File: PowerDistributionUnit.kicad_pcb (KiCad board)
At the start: 4 copper layers, 179.3 x 86.6 mm, 113 parts, among them J1.1 POWER_PINS, J1.10 RF_PINS, J1.11 EPS_PINS, J1.12 I_BAT_PINS, J1.13 I_PV_PINS, J1.2 UART_PINS, J1.3 SBW_PINS, J1.4 I2C_PINS, J1.5 30_Minute_Bypass_Jumpers, J1.6 Direct_Power_Pins, J1.7 OBC_PINS, J1.8 PL_PINS, J1.9 ACS_PINS, M1.1 PMOS, M1.2 PMOS, M1.3 NMOS, M1.4 PMOS, SW1.1 Inhibit, SW1.2 Inhibit, U1.1 LTC6995, U2.1 MSP430F5529IPN, U3.1 RT4812, U4.1 TPS62086, U5.1 TPS2557, U5.2 TPS2557, U5.3 TPS2557, U5.4 TPS2557, U6.1 MAX44284E, U6.2 MAX44284E, U6.3 MAX44284E, U6.4 MAX44284E, U6.5 MAX44284E, U6.6 MAX44284E, U6.7 MAX44284E

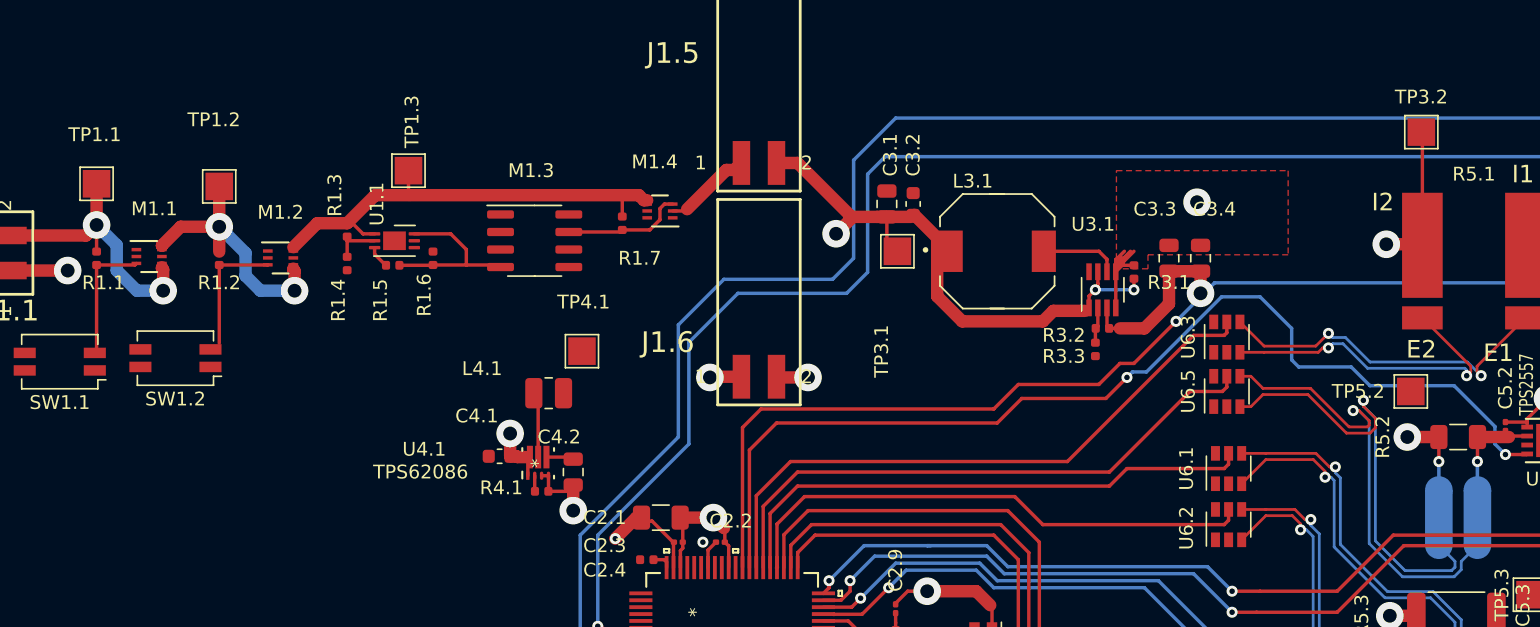
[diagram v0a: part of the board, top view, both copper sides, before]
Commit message: Adjusted power plane and added missing ground VIAs
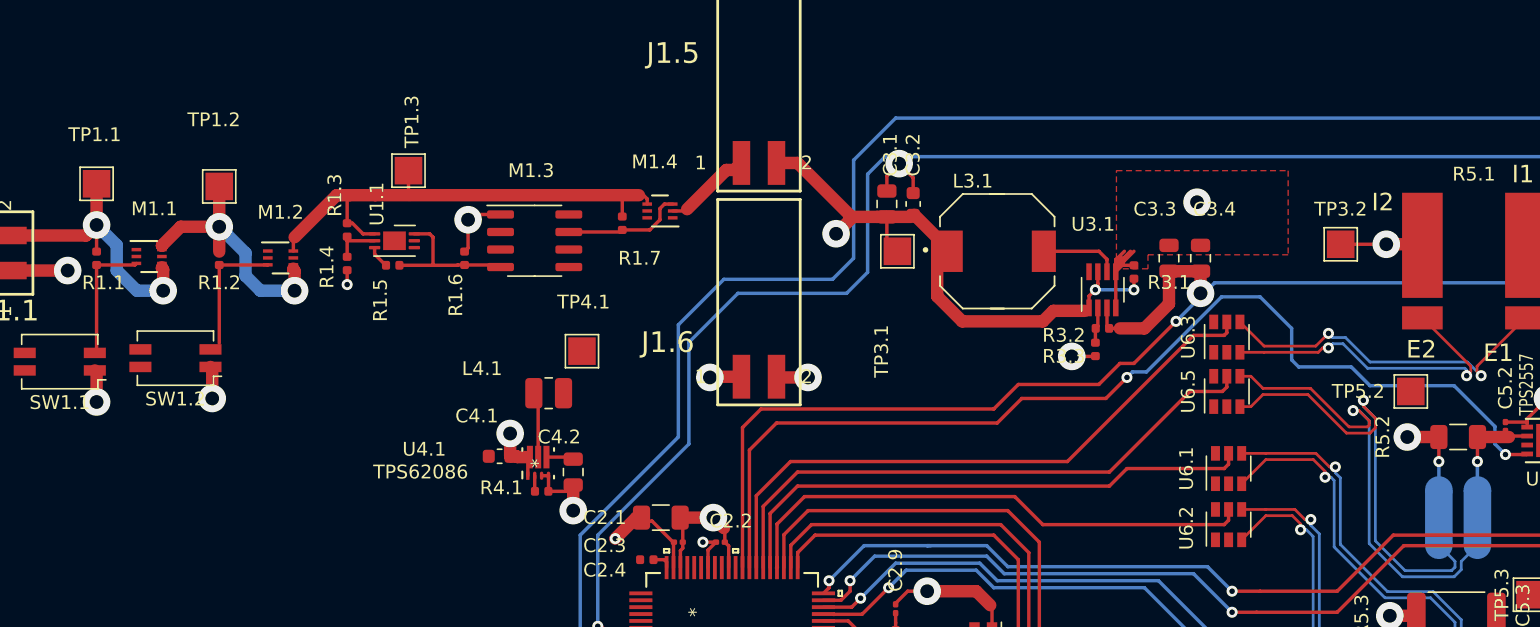
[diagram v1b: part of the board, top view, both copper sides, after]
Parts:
- moved TP3.2 10.0 mm to (174.5, 77.0)
- moved R1.6 2.29 mm to (111.0, 78.0)
- turned R1.4 to 270 degrees
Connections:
- C2.1 pad 1 (DVCC1): (no net) -> /3.3V_Regulated
- C2.2 pad 1: 3.3V_MSP -> /3.3V_Regulated
- C2.3 pad 1 (DVCC1): (no net) -> /3.3V_Regulated
- C2.5 pad 1 (VBUS): (no net) -> /5V_Regulated
- C3.1 pad 1: /30_Minute_Output -> Net-(J1.5-Pad2)
- C3.2 pad 1: /30_Minute_Output -> Net-(J1.5-Pad2)
- C4.1 pad 1: /30_Minute_Output -> Net-(J1.5-Pad2)
- J1.1 pad 1: Net-(J1.1-Pad1) -> GNDA
- J1.1 pad 2: GNDA -> Net-(J1.1-Pad1)
- J1.6 pad 1: /30_Minute_Output -> Net-(J1.5-Pad2)
- L3.1 pad 1: /30_Minute_Output -> Net-(J1.5-Pad2)
- M1.2 pad 6 (D): (no net) -> Net-(M1.2-Pad2)
- M1.3 pad 1 (S): (no net) -> GNDA
- M1.3 pad 4 (G): (no net) -> Net-(M1.3-Pad2)
- M1.4 pad 4 (S): (no net) -> Net-(M1.2-Pad2)
- R1.3 pad 1: Net-(M1.2-Pad1) -> Net-(M1.2-Pad2)
- TP3.1 pad 1: /30_Minute_Output -> Net-(J1.5-Pad2)
- U1.1 pad 6 (OUT): (no net) -> Net-(M1.3-Pad2)
- U2.1 pad 11 (AVCC1): (no net) -> /3.3V_Regulated
- U2.1 pad 14 (AVSS1): (no net) -> GNDA
- U2.1 pad 18 (DVCC1): (no net) -> /3.3V_Regulated
- U2.1 pad 65 (VBUS): (no net) -> /5V_Regulated
- U4.1 pad 1 (EN): (no net) -> Net-(J1.5-Pad2)
- U4.1 pad 7 (VIN): (no net) -> Net-(J1.5-Pad2)
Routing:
- net GNDA: track 141.6 -> 166.7 mm, vias 12 -> 19
- net 3.3V_MSP: track 11.0 -> 1.03 mm, vias 2 -> 1
- net /3.3V_Regulated: track 7.82 -> 17.8 mm, vias 2 -> 3
- net (no net): track 15.8 -> 8.31 mm, vias 1 -> 0
- net /30_Minute_Output: track 13.4 -> 6.83 mm, vias 2 -> 0
- net Net-(J1.5-Pad2): track 42.4 -> 49.0 mm, vias 3 -> 5
- net Net-(J1.1-Pad1): track 26.4 -> 21.7 mm, vias 3 -> 2
- net Net-(M1.2-Pad2): track 33.0 -> 36.1 mm
- net /5V_Regulated: track 43.0 -> 45.7 mm, vias 11 -> 12
- net GND: track 2.08 -> 0.00 mm
- net Net-(M1.3-Pad2): track 12.8 -> 10.9 mm

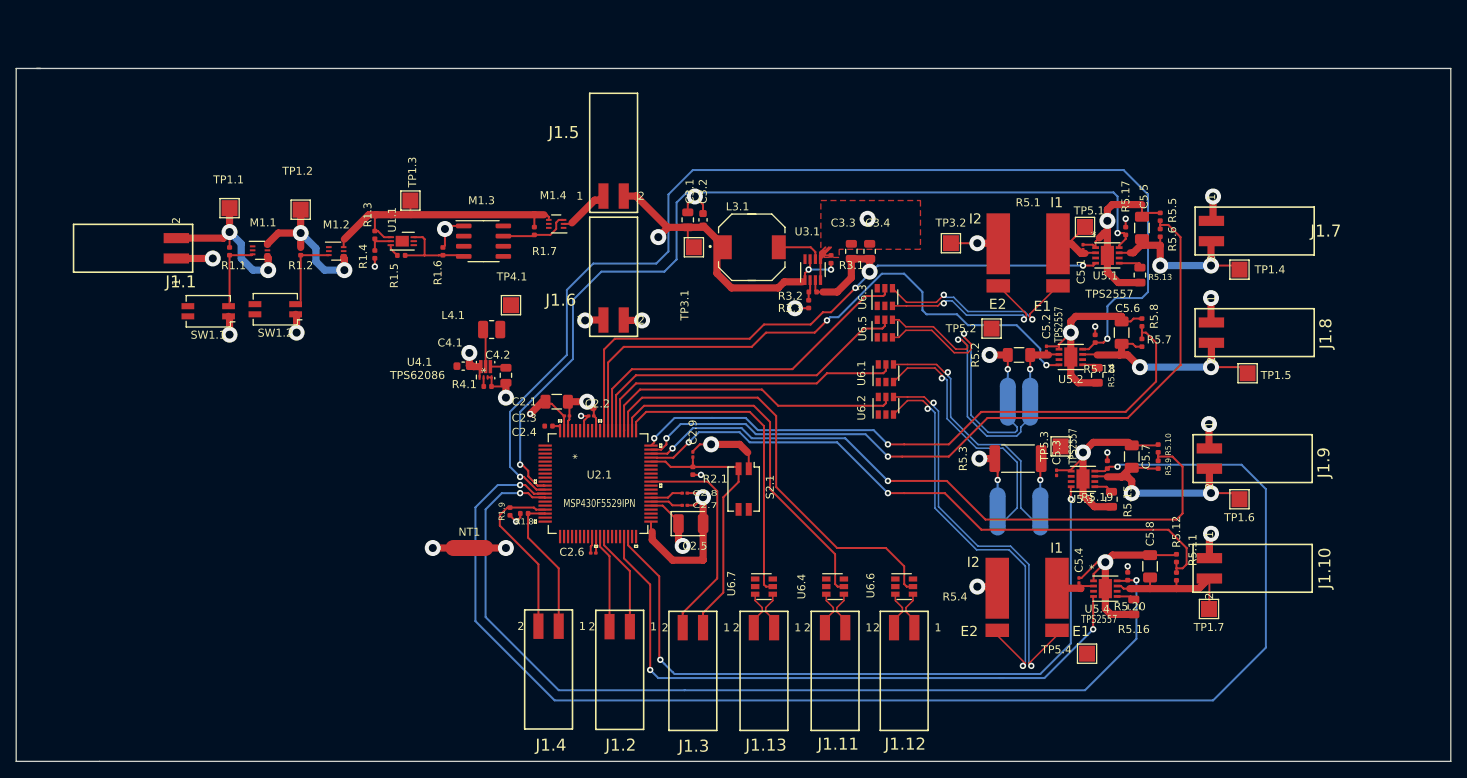
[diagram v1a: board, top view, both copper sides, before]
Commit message: Changed board outline to reflect CubeSat dimensions
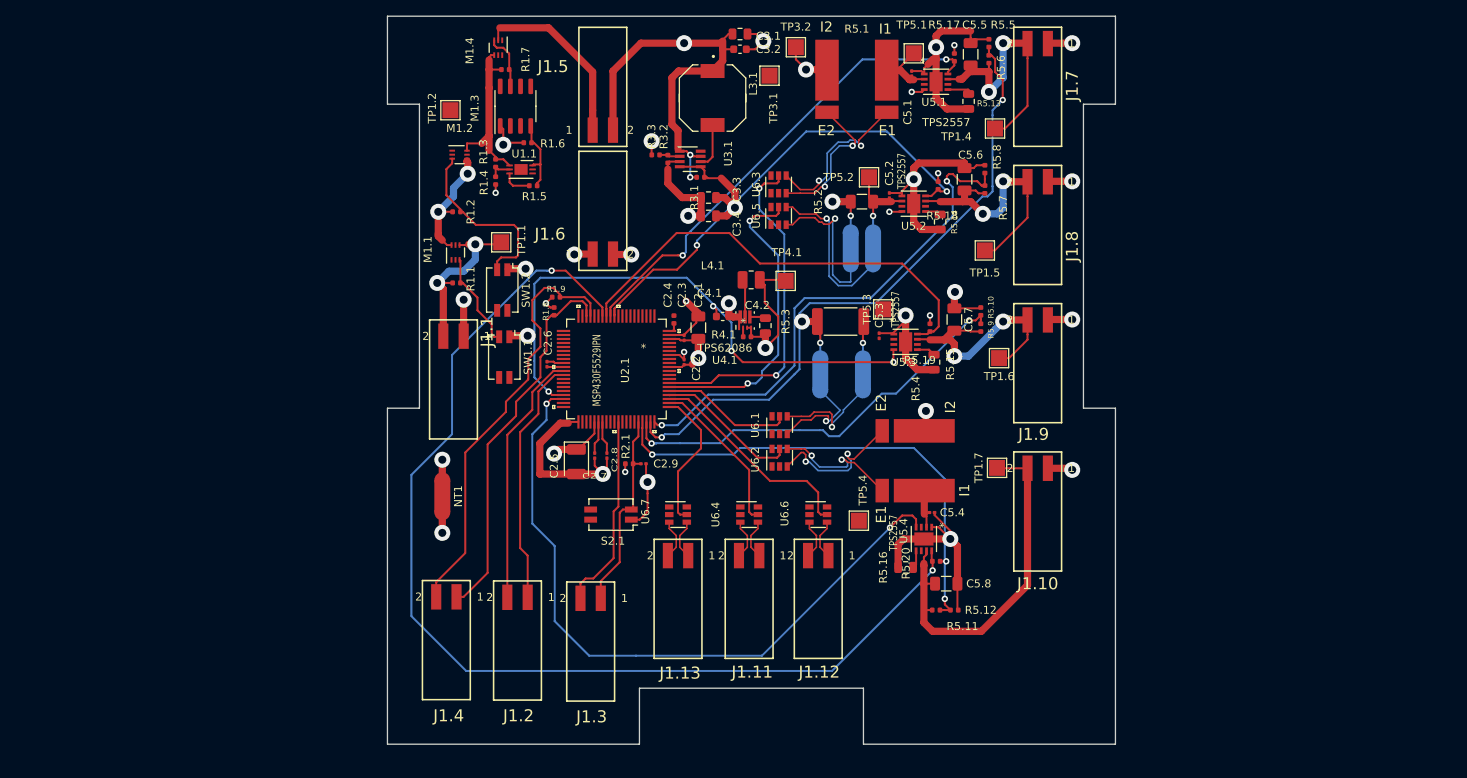
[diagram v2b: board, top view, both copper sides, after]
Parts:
- removed TP1.3: LTC_TP, TestPoint:TestPoint_Pad_2.0x2.0mm
- moved J1.1 43.1 mm to (112.3, 93.9), turned to 180 degrees
- moved SW1.1 37.4 mm to (118.7, 91.2), turned to 270 degrees
- moved TP1.5 36.3 mm to (178.7, 77.9)
- moved TP1.4 35.3 mm to (180.0, 62.6)
- moved TP1.6 34.8 mm to (180.5, 91.3)
- moved TP4.1 34.5 mm to (153.8, 81.7)
- moved TP1.1 34.2 mm to (118.3, 76.8), turned to 90 degrees
- moved L4.1 33.0 mm to (149.5, 81.5)
- moved U4.1 33.0 mm to (148.8, 86.6)
- moved C4.1 33.0 mm to (146.0, 86.1)
- moved C4.2 33.0 mm to (151.3, 87.3)
- moved R4.1 33.0 mm to (149.0, 88.7)
- moved TP5.4 33.0 mm to (163.0, 111.6), turned to 270 degrees
- moved J1.7 32.5 mm to (185.3, 57.3), turned to 180 degrees
- moved TP1.7 31.8 mm to (180.3, 105.0), turned to 270 degrees
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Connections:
- C5.8 pad 1: Net-(C5.8-Pad1) -> /SubsystemLoadSwitches/RF
- M1.1 pad 4 (S): (no net) -> Net-(J1.1-Pad1)
- M1.1 pad 6 (D): (no net) -> Net-(M1.1-Pad1)
- M1.2 pad 3 (G): (no net) -> Net-(M1.2-Pad1)
- M1.2 pad 4 (S): (no net) -> Net-(M1.1-Pad1)
- M1.3 pad 7 (D): (no net) -> Net-(M1.2-Pad1)
- M1.4 pad 2 (D): (no net) -> /30_Minute_Output
- R1.2 pad 1: Net-(M1.1-Pad1) -> Net-(M1.2-Pad1)
- R1.2 pad 2: Net-(M1.2-Pad2) -> Net-(M1.1-Pad1)
- SW1.2 pad 2: Net-(M1.2-Pad2) -> Net-(M1.2-Pad1)
- U1.1 pad 1 (V+): (no net) -> Net-(M1.2-Pad2)
- U1.1 pad 2 (DIV): (no net) -> Net-(R1.3-Pad2)
- U1.1 pad 3 (SET): (no net) -> Net-(R1.5-Pad2)
- U2.1 pad 31: /fault_OBC -> /fault_PL
- U2.1 pad 32: /fault_PL -> /fault_OBC
- U2.1 pad 57: /enable_RF -> /enable_ACS
- U2.1 pad 58: /enable_ACS -> /enable_RF
- U6.1 pad 1: +5V -> /3.3V_Regulated
- U6.1 pad 2: GNDD -> GNDA
- U6.2 pad 1: +5V -> /3.3V_Regulated
- U6.2 pad 2: GNDD -> GNDA
- U6.3 pad 1: +5V -> /3.3V_Regulated
- U6.3 pad 2: GNDD -> GNDA
- U6.4 pad 1: +5V -> /3.3V_Regulated
- U6.4 pad 2: GNDD -> GNDA
- U6.5 pad 1: +5V -> /3.3V_Regulated
- U6.5 pad 2: GNDD -> GNDA
- U6.6 pad 1: +5V -> /3.3V_Regulated
- U6.6 pad 2: GNDD -> GNDA
- U6.7 pad 1: +5V -> /3.3V_Regulated
- U6.7 pad 2: GNDD -> GNDA
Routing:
- net /fault_ACS: track 173.0 -> 56.6 mm, vias 2 -> 0
- net /fault_PL: track 140.6 -> 58.6 mm
- net /enable_PL: track 76.3 -> 1.59 mm, vias 2 -> 1
- net /enable_OBC: track 76.1 -> 1.70 mm, vias 2 -> 1
- net /fault_OBC: track 113.6 -> 60.1 mm
- net /RF-: track 51.7 -> 16.8 mm
- net /RF+: track 51.6 -> 18.5 mm
- net /Power_MSP430/3.0_SDA_I2C: track 22.0 -> 53.5 mm
- net /V_ACS: track 83.3 -> 52.4 mm
- net /Power_MSP430/3.1_SCL_I2C: track 17.8 -> 47.3 mm
- net Ibat_ADC: track 55.0 -> 27.1 mm
- net /SubsystemLoadSwitches/RF: track 18.7 -> 46.0 mm
- net /I_EPS: track 45.2 -> 19.9 mm
- net /I_ACS: track 39.4 -> 16.5 mm
- net Ipv_ADC: track 39.4 -> 17.9 mm
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- removed copper zone on In2.Cu, net /3.3V_Regulated
- removed copper zone on In2.Cu, net /5V_Regulated
- removed copper zone on F.Cu, net GNDA
- removed copper zone on In1.Cu, net GNDA
- removed copper zone on In1.Cu, net GNDD
- removed copper zone on In2.Cu, net Net-(J1.5-Pad2)
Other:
- board size 179.3 x 86.6 mm -> 91 x 91 mm
